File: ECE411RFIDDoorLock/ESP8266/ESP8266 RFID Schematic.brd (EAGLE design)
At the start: 61 x 43.8 mm, 30 parts, among them M1 SERVO, Q3 DMG341, T1 600mA/40V, T2 600mA/40V, U3 AP2112-3.3, X1 ESP-12E, X4 20329

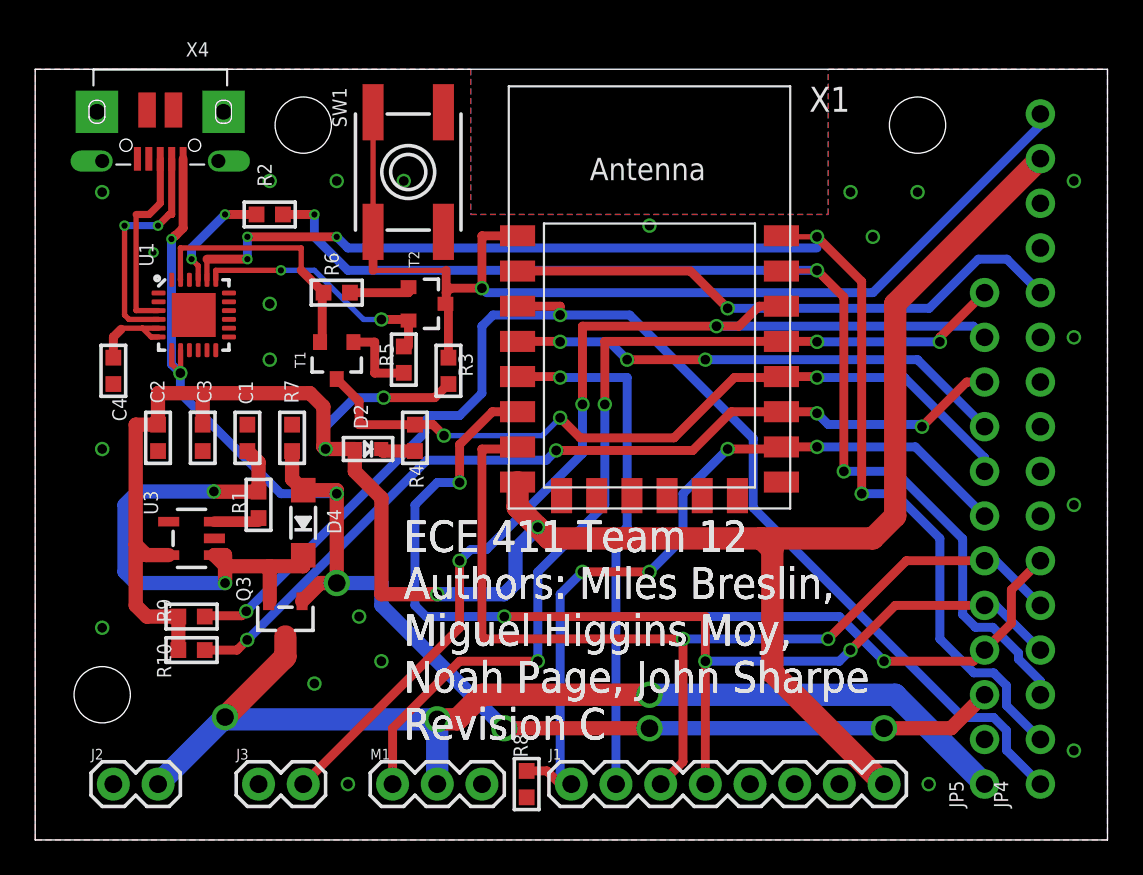
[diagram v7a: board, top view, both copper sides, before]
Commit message: added more ground stitching, iso on top pour, info layer on schematic
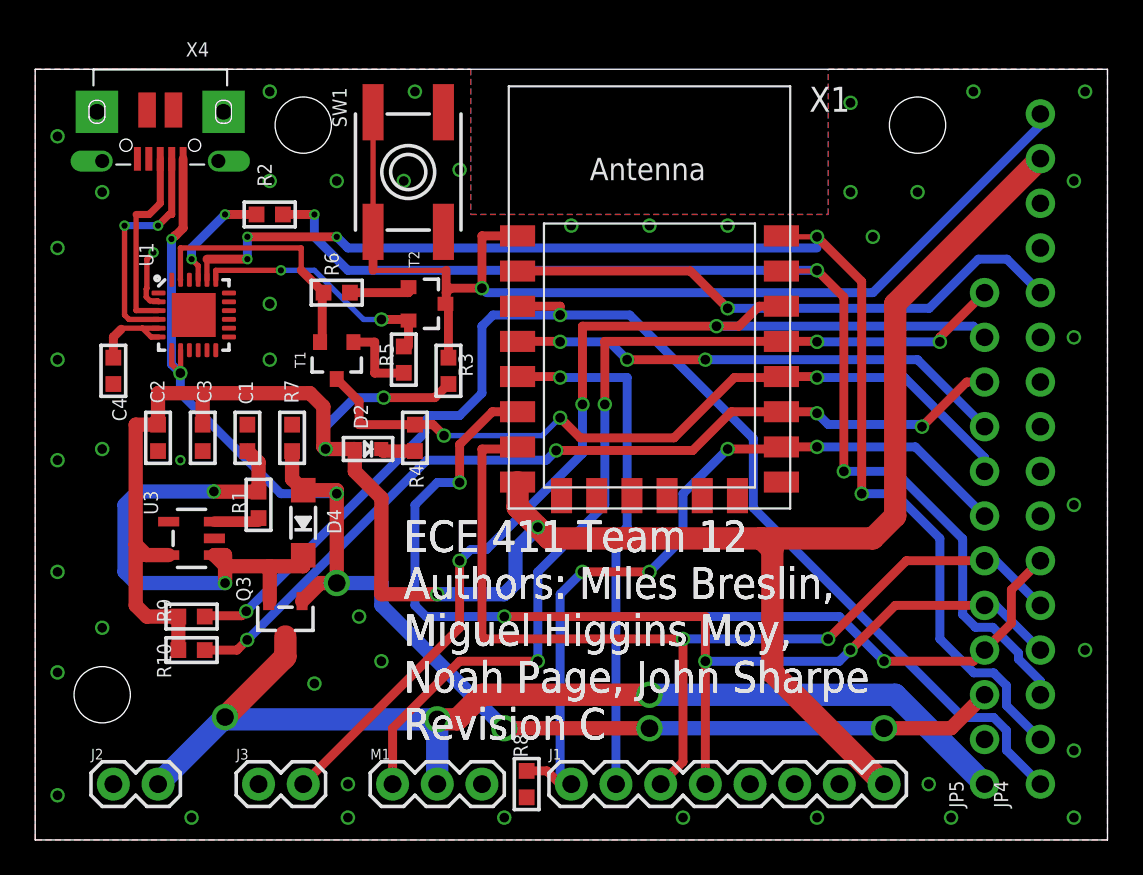
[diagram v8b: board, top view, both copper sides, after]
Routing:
- net GND: track 0.00 -> 3.52 mm, vias 1 -> 46
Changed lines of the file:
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@@
 </polygon>
 <contactref element="R8" pad="1"/>
-<polygon width="0.1524" layer="1">
+<polygon width="0.1524" layer="1" isolate="0.3048">
 <vertex x="0" y="43.815"/>
 <vertex x="24.765" y="43.815"/>
@@
 </polygon>
 <via x="6.731" y="33.401" extent="1-16" drill="0.35"/>
+<wire x1="7.017" y1="30.595" x2="6.9618" y2="30.6502" width="0.3048" layer="1"/>
+<wire x1="6.9618" y1="30.6502" x2="6.53175" y2="30.6502" width="0.3048" layer="1"/>
+<wire x1="6.53175" y1="30.6502" x2="6.3122" y2="30.86975" width="0.3048" layer="1"/>
+<wire x1="6.3122" y1="30.86975" x2="6.3122" y2="31.32025" width="0.3048" layer="1"/>
+<wire x1="6.3122" y1="31.32025" x2="6.35" y2="31.35805" width="0.3048" layer="1"/>
+<wire x1="6.35" y1="33.02" x2="6.731" y2="33.401" width="0.3048" layer="1"/>
+<wire x1="6.35" y1="31.35805" x2="6.35" y2="33.02" width="0.3048" layer="1"/>
+<via x="8.255" y="21.59" extent="1-16" drill="0.35"/>
+<via x="3.81" y="12.065" extent="1-16" drill="0.55"/>
+<via x="17.78" y="3.175" extent="1-16" drill="0.55"/>
+<via x="15.875" y="8.89" extent="1-16" drill="0.55"/>
+<via x="18.415" y="12.7" extent="1-16" drill="0.55"/>
+<via x="19.685" y="10.16" extent="1-16" drill="0.55"/>
+<via x="3.81" y="22.225" extent="1-16" drill="0.55"/>
+<via x="13.335" y="27.305" extent="1-16" drill="0.55"/>
+<via x="13.335" y="30.48" extent="1-16" drill="0.55"/>
+<via x="3.81" y="36.83" extent="1-16" drill="0.55"/>
+<via x="13.335" y="37.465" extent="1-16" drill="0.55"/>
+<via x="17.145" y="37.465" extent="1-16" drill="0.55"/>
+<via x="20.955" y="37.465" extent="1-16" drill="0.55"/>
+<via x="34.925" y="34.925" extent="1-16" drill="0.55"/>
+<via x="46.355" y="36.83" extent="1-16" drill="0.55"/>
+<via x="47.625" y="34.29" extent="1-16" drill="0.55"/>
+<via x="50.165" y="36.83" extent="1-16" drill="0.55"/>
+<via x="59.055" y="37.465" extent="1-16" drill="0.55"/>
+<via x="59.055" y="28.575" extent="1-16" drill="0.55"/>
+<via x="59.055" y="19.05" extent="1-16" drill="0.55"/>
+<via x="59.055" y="5.08" extent="1-16" drill="0.55"/>
+<via x="50.8" y="3.175" extent="1-16" drill="0.55"/>
+<via x="1.27" y="33.655" extent="1-16" drill="0.55"/>
+<via x="1.27" y="27.305" extent="1-16" drill="0.55"/>
+<via x="1.27" y="21.59" extent="1-16" drill="0.55"/>
+<via x="1.27" y="40.005" extent="1-16" drill="0.55"/>
+<via x="13.335" y="42.545" extent="1-16" drill="0.55"/>
+<via x="21.59" y="42.545" extent="1-16" drill="0.55"/>
+<via x="24.13" y="38.1" extent="1-16" drill="0.55"/>
+<via x="30.48" y="34.925" extent="1-16" drill="0.55"/>
+<via x="39.37" y="34.925" extent="1-16" drill="0.55"/>
+<via x="46.355" y="41.91" extent="1-16" drill="0.55"/>
+<via x="53.34" y="42.545" extent="1-16" drill="0.55"/>
+<via x="59.69" y="42.545" extent="1-16" drill="0.55"/>
+<via x="59.69" y="10.795" extent="1-16" drill="0.55"/>
+<via x="59.055" y="1.27" extent="1-16" drill="0.55"/>
+<via x="52.07" y="1.27" extent="1-16" drill="0.55"/>
+<via x="44.45" y="1.27" extent="1-16" drill="0.55"/>
+<via x="36.83" y="1.27" extent="1-16" drill="0.55"/>
+<via x="26.67" y="1.27" extent="1-16" drill="0.55"/>
+<via x="17.78" y="1.27" extent="1-16" drill="0.55"/>
+<via x="8.89" y="1.27" extent="1-16" drill="0.55"/>
+<via x="1.27" y="2.54" extent="1-16" drill="0.55"/>
+<via x="1.27" y="9.525" extent="1-16" drill="0.55"/>
+<via x="1.27" y="15.24" extent="1-16" drill="0.55"/>
 </signal>
 <signal name="VBAT" class="3">
@@
 <contactref element="JP5" pad="2"/>
 </signal>
-<signal name="N$1">
-<via x="3.81" y="12.065" extent="1-16" drill="0.55"/>
-</signal>
-<signal name="N$2">
-<via x="3.81" y="22.225" extent="1-16" drill="0.55"/>
-</signal>
-<signal name="N$9">
-<via x="3.81" y="36.83" extent="1-16" drill="0.55"/>
-</signal>
-<signal name="N$11">
-<via x="17.145" y="37.465" extent="1-16" drill="0.55"/>
-</signal>
-<signal name="N$15">
-<via x="13.335" y="37.465" extent="1-16" drill="0.55"/>
-</signal>
-<signal name="N$16">
-<via x="20.955" y="37.465" extent="1-16" drill="0.55"/>
-</signal>
-<signal name="N$17">
-<via x="46.355" y="36.83" extent="1-16" drill="0.55"/>
-</signal>
-<signal name="N$18">
-<via x="50.165" y="36.83" extent="1-16" drill="0.55"/>
-</signal>
-<signal name="N$19">
-<via x="47.625" y="34.29" extent="1-16" drill="0.55"/>
-</signal>
-<signal name="N$20">
-<via x="50.8" y="3.175" extent="1-16" drill="0.55"/>
-</signal>
-<signal name="N$21">
-<via x="59.055" y="37.465" extent="1-16" drill="0.55"/>
-</signal>
-<signal name="N$22">
-<via x="59.055" y="28.575" extent="1-16" drill="0.55"/>
-</signal>
-<signal name="N$23">
-<via x="59.055" y="19.05" extent="1-16" drill="0.55"/>
-</signal>
-<signal name="N$24">
-<via x="59.055" y="5.08" extent="1-16" drill="0.55"/>
-</signal>
-<signal name="N$25">
-<via x="17.78" y="3.175" extent="1-16" drill="0.55"/>
-</signal>
-<signal name="N$26">
-<via x="18.415" y="12.7" extent="1-16" drill="0.55"/>
-</signal>
-<signal name="N$27">
-<via x="15.875" y="8.89" extent="1-16" drill="0.55"/>
-</signal>
-<signal name="N$28">
-<via x="19.685" y="10.16" extent="1-16" drill="0.55"/>
-</signal>
-<signal name="N$29">
-<via x="13.335" y="27.305" extent="1-16" drill="0.55"/>
-</signal>
-<signal name="N$30">
-<via x="13.335" y="30.48" extent="1-16" drill="0.55"/>
-</signal>
-<signal name="N$31">
-<via x="34.925" y="34.925" extent="1-16" drill="0.55"/>
-</signal>
 </signals>
